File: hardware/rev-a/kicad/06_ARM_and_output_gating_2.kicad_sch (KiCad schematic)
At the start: 1 part

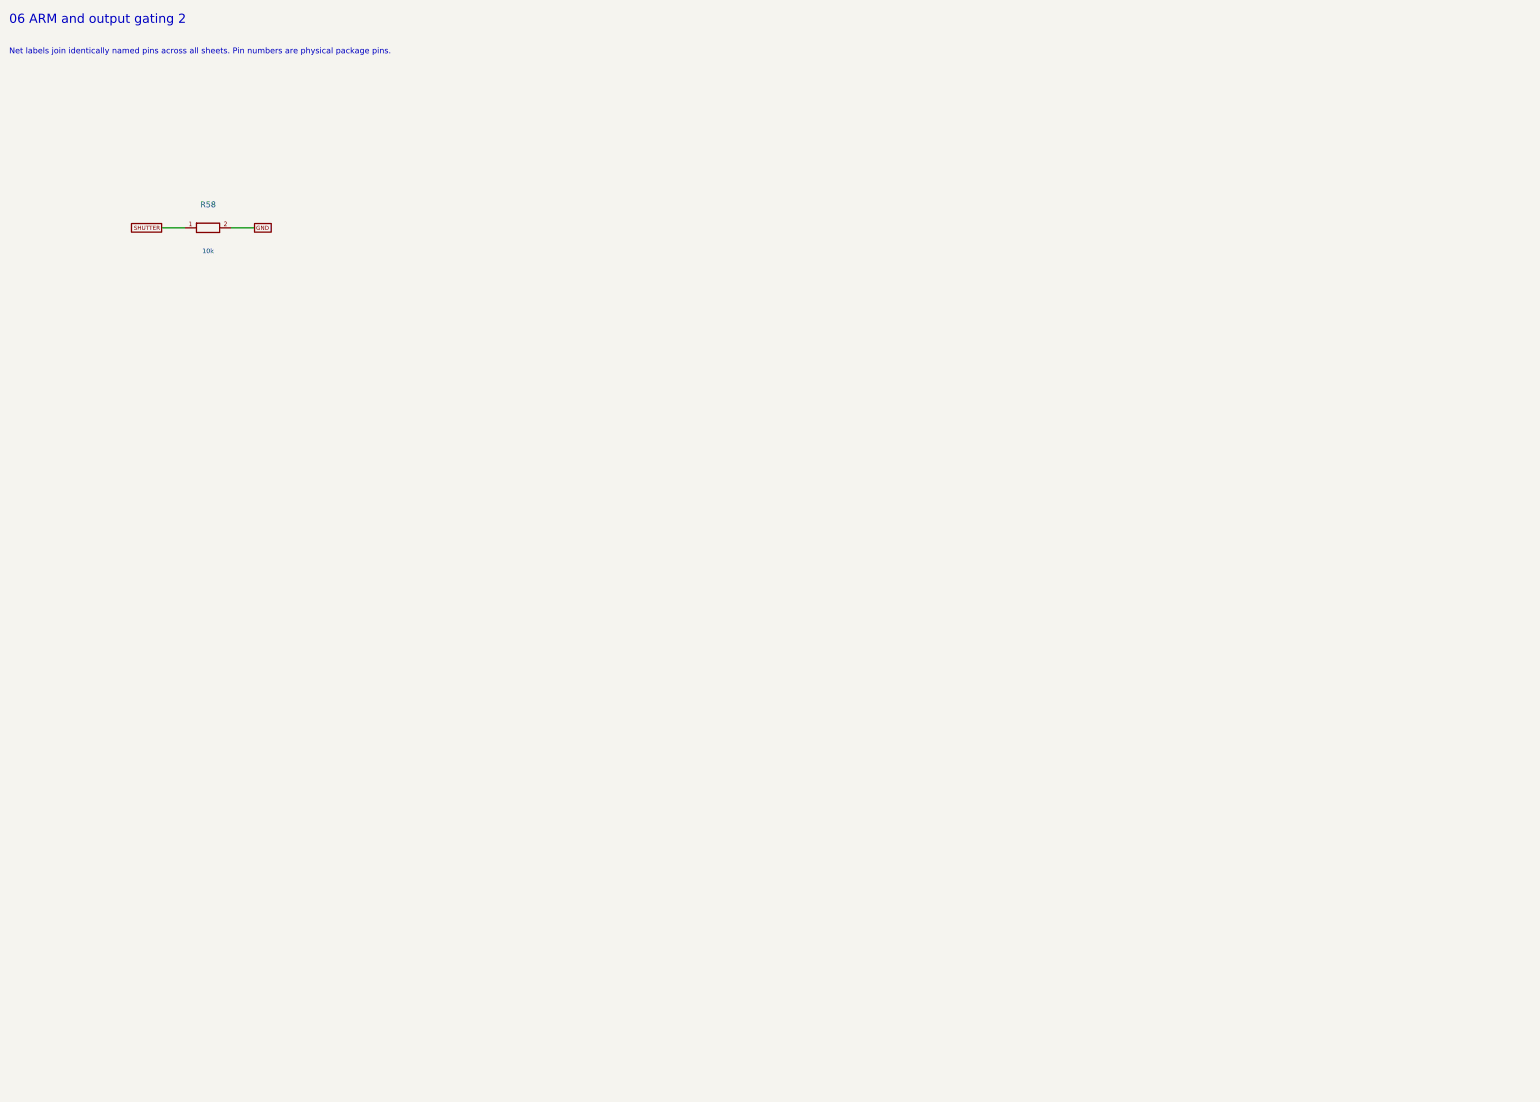
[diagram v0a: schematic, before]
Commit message: Redraw Rev.A schematics with functional blocks and explicit wiring
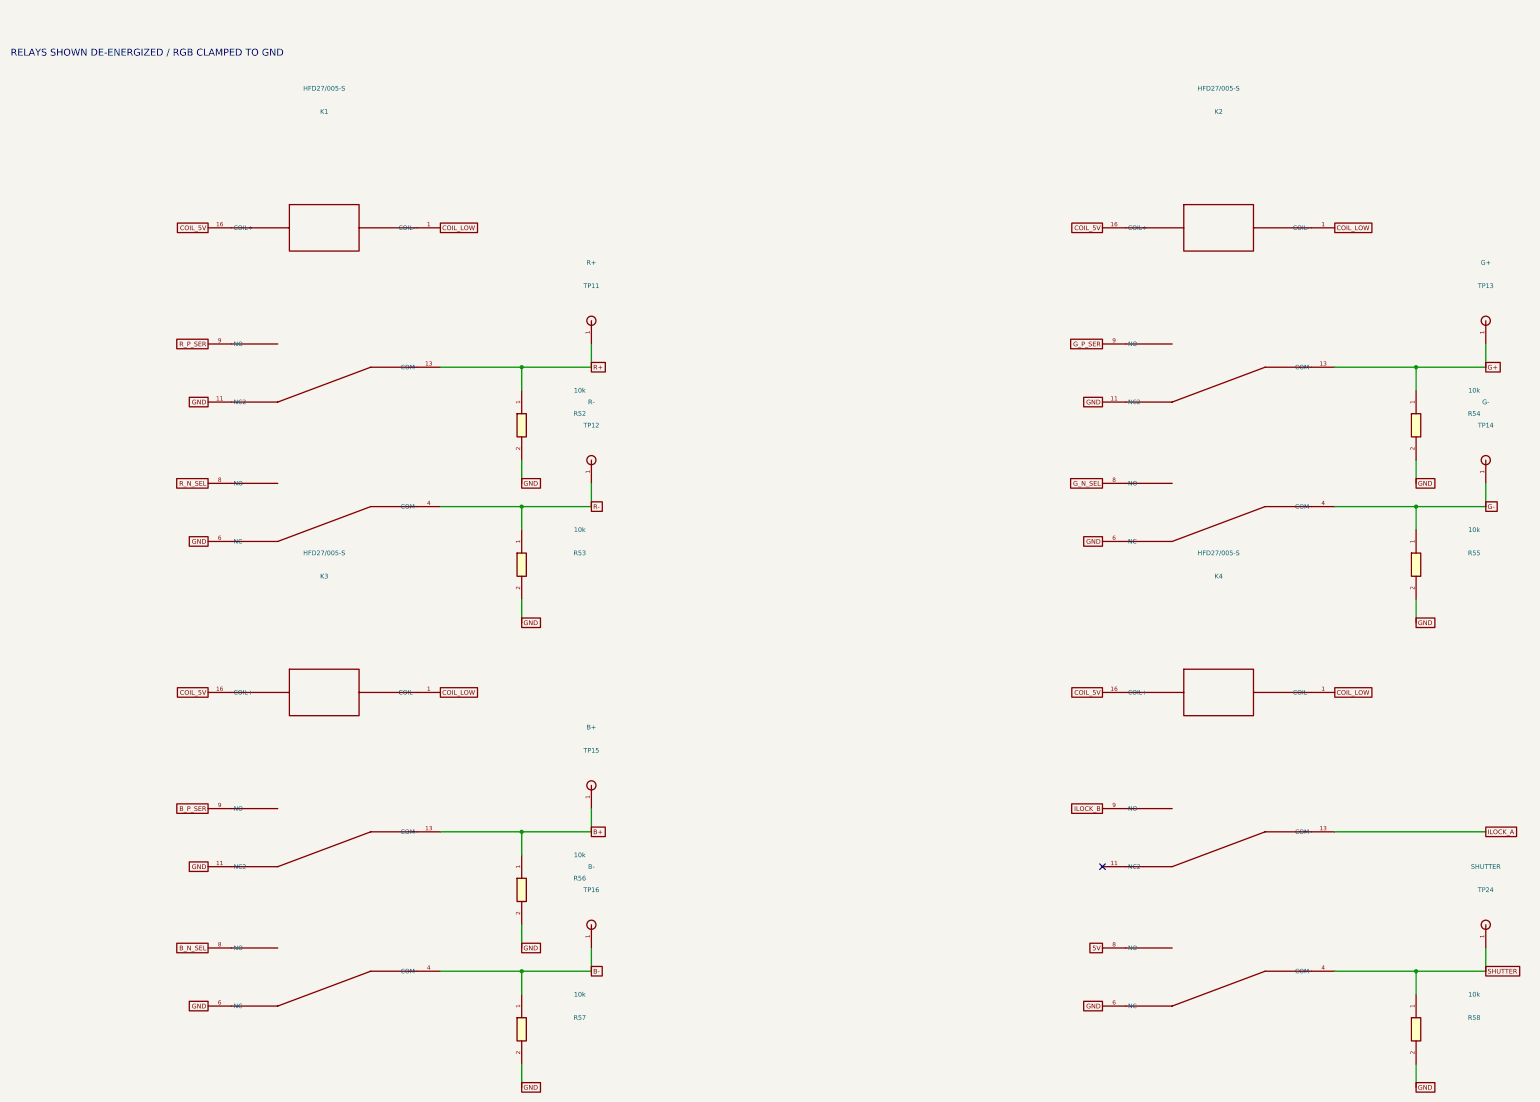
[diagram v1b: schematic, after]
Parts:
- added K1: HFD27/005-S, RevA:HFD27, symbol RevA:Part_K1
- added K2: HFD27/005-S, RevA:HFD27, symbol RevA:Part_K2
- added K3: HFD27/005-S, RevA:HFD27, symbol RevA:Part_K3
- added K4: HFD27/005-S, RevA:HFD27, symbol RevA:Part_K4
- added R52, R53, R54, R55, R56, R57: 10k, RevA:R_Axial_DIN0207_L6.3mm_D2.5mm_P10.16mm_Horizontal, symbol RevA:R
- added TP11: R+, RevA:TestPoint_THTPad_D2.0mm_Drill1.0mm, symbol RevA:TP
- added TP12: R-, RevA:TestPoint_THTPad_D2.0mm_Drill1.0mm, symbol RevA:TP
- added TP13: G+, RevA:TestPoint_THTPad_D2.0mm_Drill1.0mm, symbol RevA:TP
- added TP14: G-, RevA:TestPoint_THTPad_D2.0mm_Drill1.0mm, symbol RevA:TP
- added TP15: B+, RevA:TestPoint_THTPad_D2.0mm_Drill1.0mm, symbol RevA:TP
- added TP16: B-, RevA:TestPoint_THTPad_D2.0mm_Drill1.0mm, symbol RevA:TP
- added TP24: SHUTTER, RevA:TestPoint_THTPad_D2.0mm_Drill1.0mm, symbol RevA:TP
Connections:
- net GND: now also K1.11 (NC2), K1.6 (NC), K2.11 (NC2), K2.6 (NC), K3.11 (NC2), K3.6 (NC), K4.6 (NC), R52.2, R53.2, R54.2, R55.2, R56.2, R57.2
- net SHUTTER: now also K4.4 (COM), TP24.1
- new net 5V: K4.8 (NO)
- new net B+: K3.13 (COM), R56.1, TP15.1
- new net B-: K3.4 (COM), R57.1, TP16.1
- new net B_N_SEL: K3.8 (NO)
- new net B_P_SER: K3.9 (NO)
- new net COIL_5V: K1.16 (COIL+), K2.16 (COIL+), K3.16 (COIL+), K4.16 (COIL+)
- new net COIL_LOW: K1.1 (COIL-), K2.1 (COIL-), K3.1 (COIL-), K4.1 (COIL-)
- new net G+: K2.13 (COM), R54.1, TP13.1
- new net G-: K2.4 (COM), R55.1, TP14.1
- new net G_N_SEL: K2.8 (NO)
- new net G_P_SER: K2.9 (NO)
- new net ILOCK_A: K4.13 (COM)
- new net ILOCK_B: K4.9 (NO)
- new net R+: K1.13 (COM), R52.1, TP11.1
- new net R-: K1.4 (COM), R53.1, TP12.1
- new net R_N_SEL: K1.8 (NO)
- new net R_P_SER: K1.9 (NO)
- no-connect marks 0 -> 1
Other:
- note added: "RELAYS SHOWN DE-ENERGIZED / RGB CLAMPED TO GND"
- note removed: "06 ARM and output gating 2"
- note removed: "Net labels join identically named pins across all sheets. Pin numbers are physical package pins."
- company: CoreS3 ILDA evaluation -> (none)
- title: 06_ARM_and_output_gating_2 -> 11 / Fail-off relay contacts
